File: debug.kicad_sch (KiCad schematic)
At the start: 61 parts, among them J701 USB4105-GF-A, J702 Conn_02x10_Odd_Even, U701 USBLC6-2SC6, U702 FT231XQ-R, U703 TCA9554PW

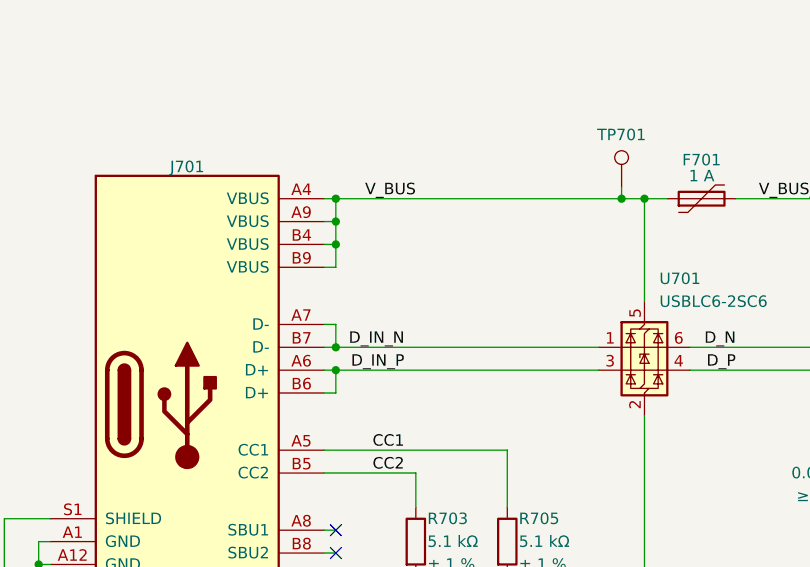
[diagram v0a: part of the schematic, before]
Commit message: Redo MPU pinout using STM32CubeMx
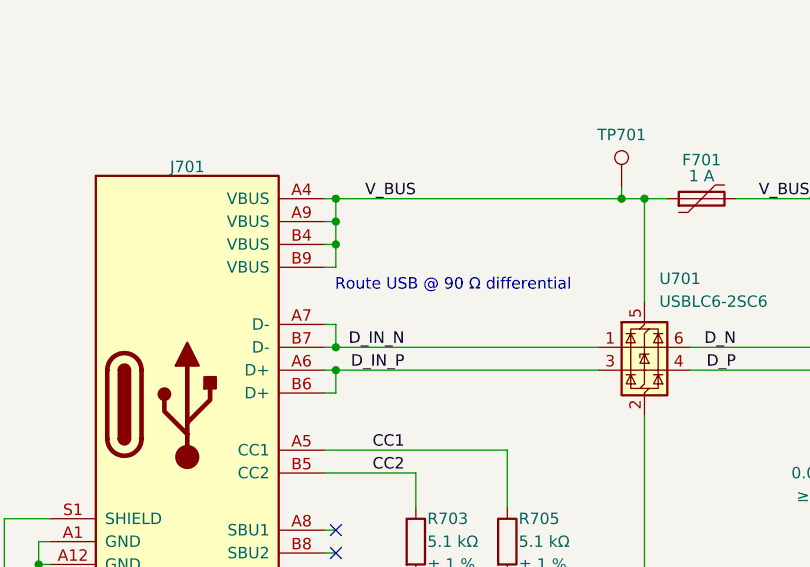
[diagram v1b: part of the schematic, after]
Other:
- note added: "Route USB @ 90 Ω differential"
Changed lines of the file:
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@@
 		(rev "v0.0.1")
+	)
+	(text "Route USB @ 90 Ω differential"
+		(exclude_from_sim no)
+		(at 80.772 200.152 0)
+		(effects
+			(font
+				(size 1.27 1.27)
+				(color 194 0 194 1)
+			)
+			(justify right)
+		)
 	)
 	(text_box "There are 4 debug LEDs; two RGB LEDs and two red LEDs."

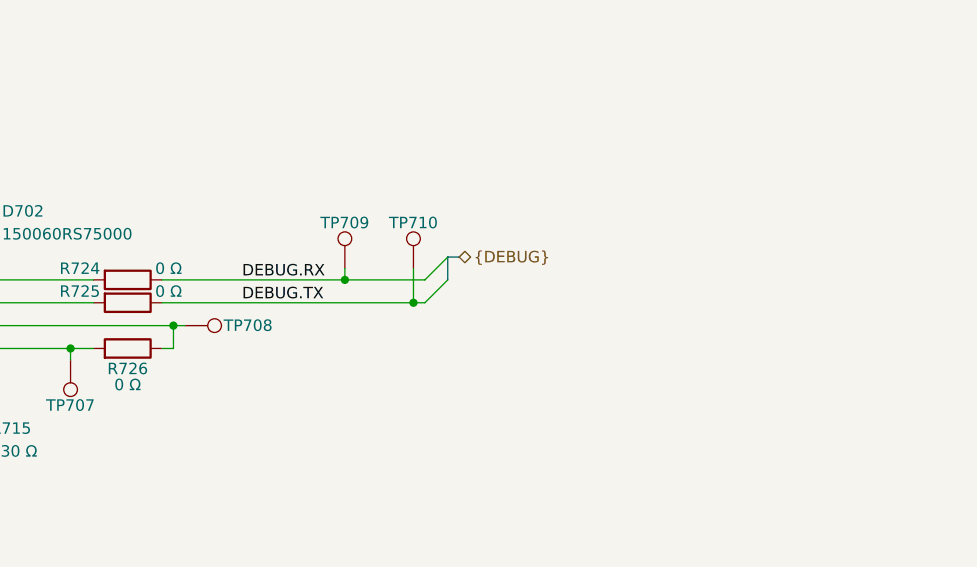
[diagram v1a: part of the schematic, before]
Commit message: Add debug VCOM port 0 ohm pokayoke
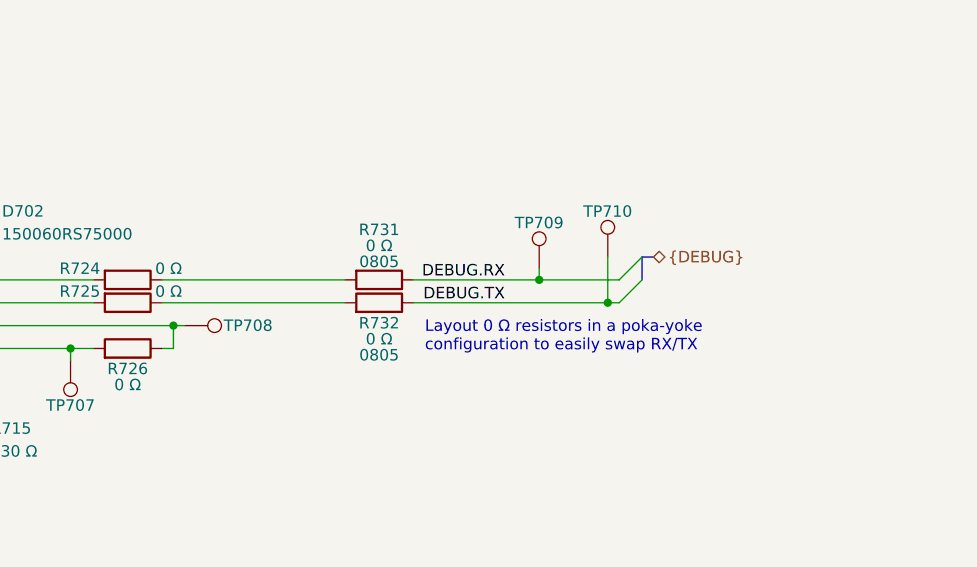
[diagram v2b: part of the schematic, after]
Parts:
- added R724: 0 Ω, perfect_footprints:R_0402_1005Metric, symbol Device:R
- added R732: 0 Ω, Resistor_SMD:R_0805_2012Metric, symbol Device:R
- R731: renamed from R724; footprint perfect_footprints:R_0402_1005Metric -> Resistor_SMD:R_0805_2012Metric; MPN 560112110020 -> (none); Manufacturer Würth Elektronik -> (none); Size (none) -> 0805
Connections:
- net DEBUG.TX: now also R732.1; no longer R725.1
- net TXD: now also R724.2; no longer R731.2
- new net: R725.1, R732.2
- new net: R724.1, R731.2
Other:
- note added: "Layout 0 Ω resistors in a poka-yoke configuration to easily swap RX/TX"
- moved on the sheet: R731, TP709, TP710

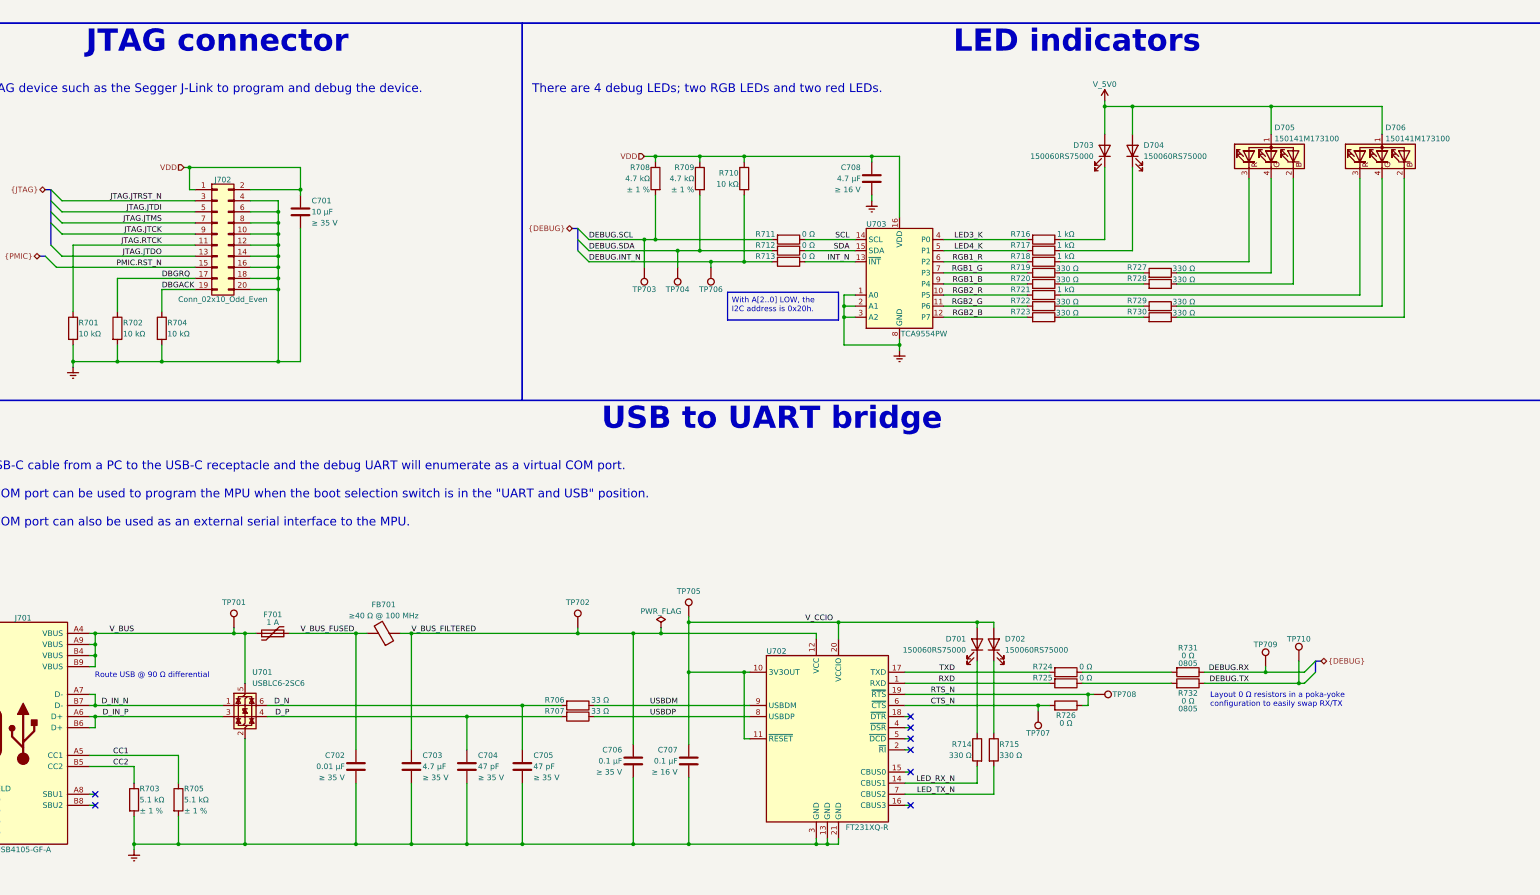
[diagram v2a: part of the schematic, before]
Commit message: Add additional info to passives
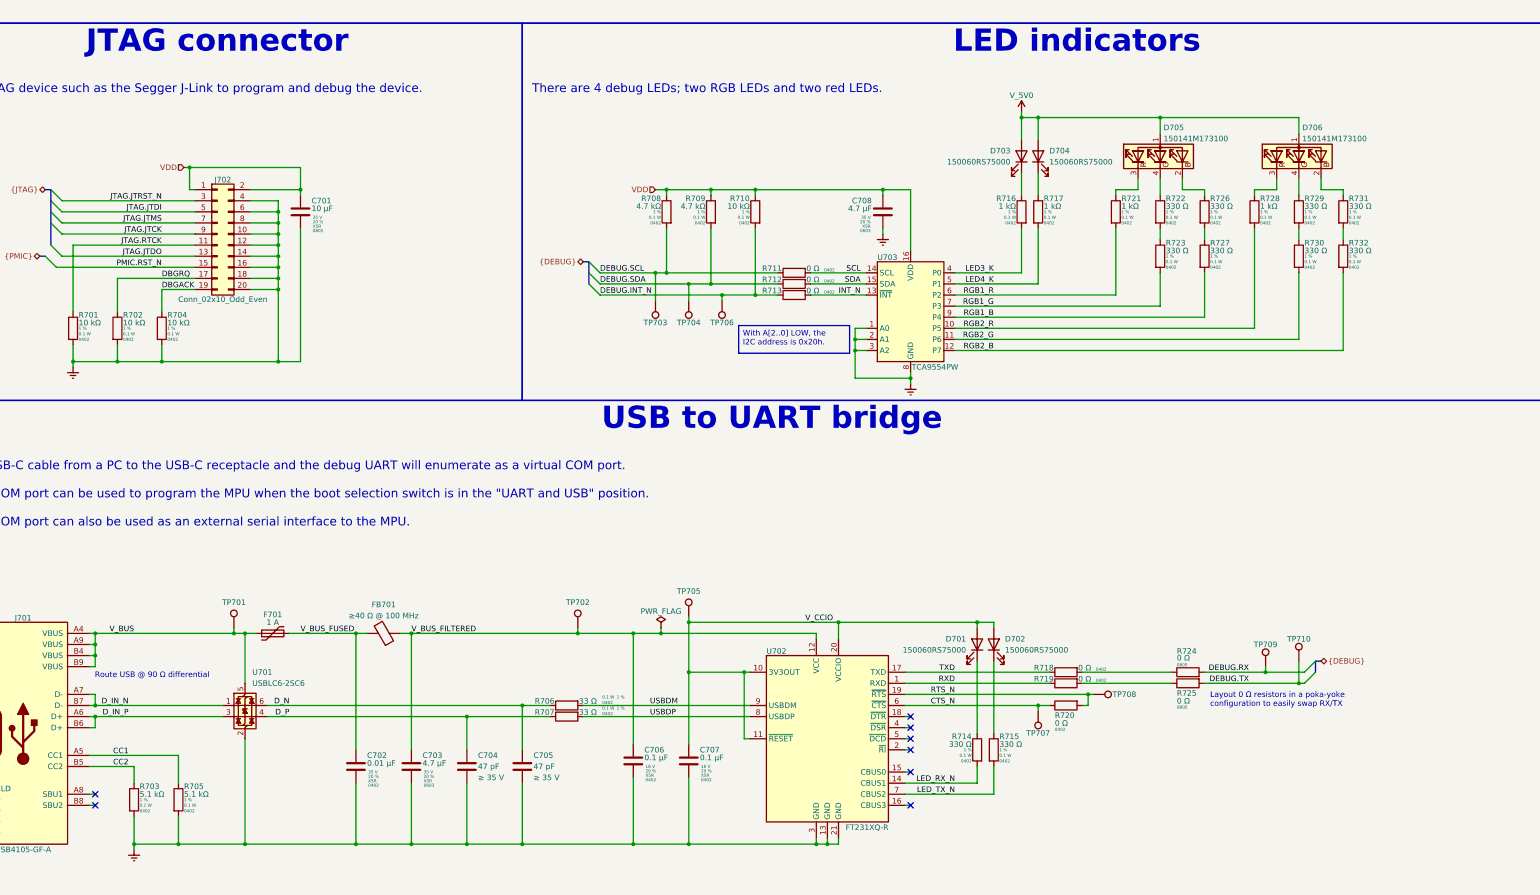
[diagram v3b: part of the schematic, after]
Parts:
- C701: footprint Capacitor_SMD:C_0603_1608Metric -> (none); MPN GRM188R6YA106MA73D -> (none); Manufacturer Murata Electronics -> (none); Size (none) -> 0805; Temperature coefficient (none) -> X5R; Tolerance (none) -> 20 %; Voltage rating ≥ 35 V -> 35 V
- C702: Size (none) -> 0402; Temperature coefficient (none) -> X5R; Tolerance (none) -> 20 %; Voltage rating ≥ 35 V -> 35 V
- C703: footprint Capacitor_SMD:C_0603_1608Metric -> (none); MPN GRM188R6YA475KE15D -> (none); Manufacturer Murata Electronics -> (none); Size (none) -> 0603; Temperature coefficient (none) -> X5R; Tolerance (none) -> 20 %; Voltage rating ≥ 35 V -> 35 V
- C706: Size (none) -> 0402; Temperature coefficient (none) -> X5R; Tolerance (none) -> 20 %; Voltage rating ≥ 35 V -> 16 V
- C707: Size (none) -> 0402; Temperature coefficient (none) -> X5R; Tolerance (none) -> 20 %; Voltage rating ≥ 16 V -> 16 V
- C708: footprint Capacitor_SMD:C_0603_1608Metric -> (none); MPN GRM188R6YA475KE15D -> (none); Manufacturer Murata Electronics -> (none); Size (none) -> 0603; Temperature coefficient (none) -> X5R; Tolerance (none) -> 20 %; Voltage rating ≥ 16 V -> 35 V
- R701, R702, R704, R706, R707, R710, R716, R717, R721: MPN 560112110020 -> (none); Manufacturer Würth Elektronik -> (none); Power rating (none) -> 0.1 W; Size (none) -> 0402; Tolerance (none) -> 1 %
- R703, R705, R708, R709: Power rating (none) -> 0.1 W; Size (none) -> 0402; Tolerance ± 1 % -> 1 %
- R711, R712, R713: footprint perfect_footprints:R_0402_1005Metric -> (none); MPN 560112110020 -> (none); Manufacturer Würth Elektronik -> (none); Size (none) -> 0402
- R714, R715, R722, R723, R727, R729, R730: MPN 560112110019 -> (none); Manufacturer Würth Elektronik -> (none); Power rating (none) -> 0.1 W; Size (none) -> 0402; Tolerance (none) -> 1 %
- R718: value 1 kΩ -> 0 Ω; footprint perfect_footprints:R_0402_1005Metric -> (none); MPN 560112110020 -> (none); Manufacturer Würth Elektronik -> (none); Size (none) -> 0402
- R719, R720: value 330 Ω -> 0 Ω; footprint perfect_footprints:R_0402_1005Metric -> (none); MPN 560112110019 -> (none); Manufacturer Würth Elektronik -> (none); Size (none) -> 0402
- R724, R725: footprint perfect_footprints:R_0402_1005Metric -> (none); MPN 560112110020 -> (none); Manufacturer Würth Elektronik -> (none); Size (none) -> 0805
- R726: value 0 Ω -> 330 Ω; footprint Resistor_SMD:R_0805_2012Metric -> perfect_footprints:R_0402_1005Metric; MPN 560112120002 -> (none); Manufacturer Würth Elektronik -> (none); Power rating (none) -> 0.1 W; Size (none) -> 0402; Tolerance (none) -> 1 %
- R728: value 330 Ω -> 1 kΩ; MPN 560112110019 -> (none); Manufacturer Würth Elektronik -> (none); Power rating (none) -> 0.1 W; Size (none) -> 0402; Tolerance (none) -> 1 %
- R731, R732: value 0 Ω -> 330 Ω; footprint Resistor_SMD:R_0805_2012Metric -> perfect_footprints:R_0402_1005Metric; Power rating (none) -> 0.1 W; Size 0805 -> 0402; Tolerance (none) -> 1 %
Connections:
- net CTS_N: now also R720.1; no longer R726.2
- net DEBUG.INT_N: now also R713.1; no longer R713.2
- net DEBUG.RX: now also R724.2; no longer R731.1
- net DEBUG.SCL: now also R711.1; no longer R711.2
- net DEBUG.SDA: now also R712.1; no longer R712.2
- net DEBUG.TX: now also R725.2; no longer R732.1
- net D_N: now also R706.1; no longer R706.2
- net D_P: now also R707.1; no longer R707.2
- net INT_N: now also R713.2; no longer R713.1
- net RGB1_B: now also R727.2; no longer R720.2
- net RGB1_G: now also R723.2; no longer R719.2
- net RGB1_R: now also R721.2; no longer R718.2
- net RGB2_B: now also R732.2; no longer R723.2
- net RGB2_G: now also R730.2; no longer R722.2
- net RGB2_R: now also R728.2; no longer R721.2
- net RTS_N: now also R720.2; no longer R726.1
- net RXD: now also R719.1; no longer R725.2
- net SCL: now also R711.2; no longer R711.1
- net SDA: now also R712.2; no longer R712.1
- net TXD: now also R718.1; no longer R724.2
- net USBDM: now also R706.2; no longer R706.1
- net USBDP: now also R707.2; no longer R707.1
- net at R725.1: now also R719.2; no longer R732.2
- net at R722.1: now also D705.4 (GK); no longer R729.2
- net at D705.2 (BK): now also R726.1; no longer R728.1
- net at D705.3 (RK): now also R721.1; no longer R718.1
- net at R727.1: now also R726.2; no longer D705.4 (GK)
- net at R730.1: now also R729.2; no longer D706.2 (BK)
- net at R723.1: now also R722.2; no longer R730.2
- net at R724.1: now also R718.2; no longer R731.2
- net at D706.3 (RK): now also R728.1; no longer R721.1
- new net: R731.2, R732.1
- new net: D706.2 (BK), R731.1
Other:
- moved on the sheet: D703, D705, TP703, TP704, TP706, U703

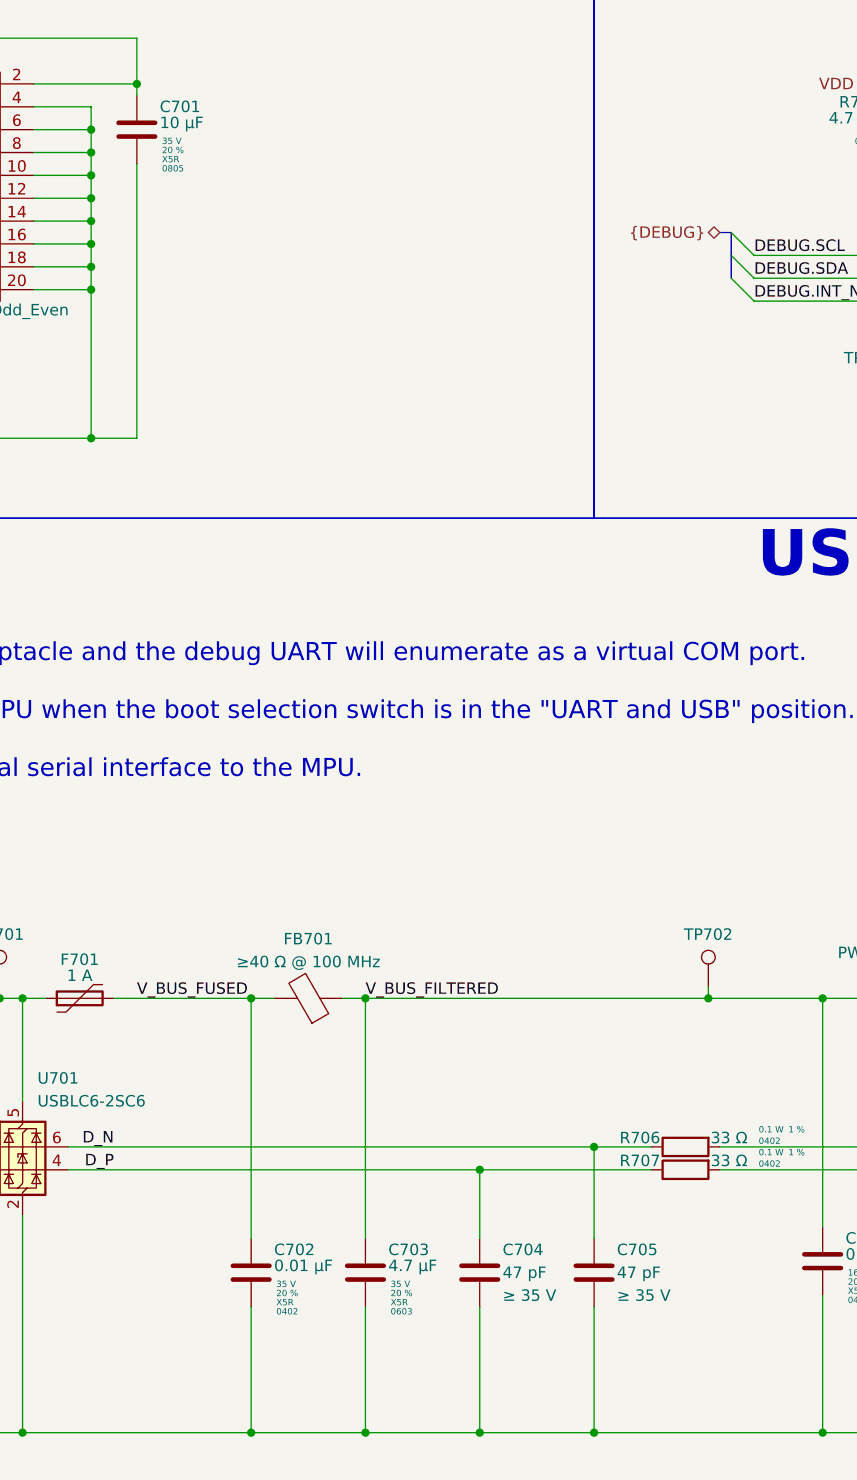
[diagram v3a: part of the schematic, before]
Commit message: Update capacitor BOM
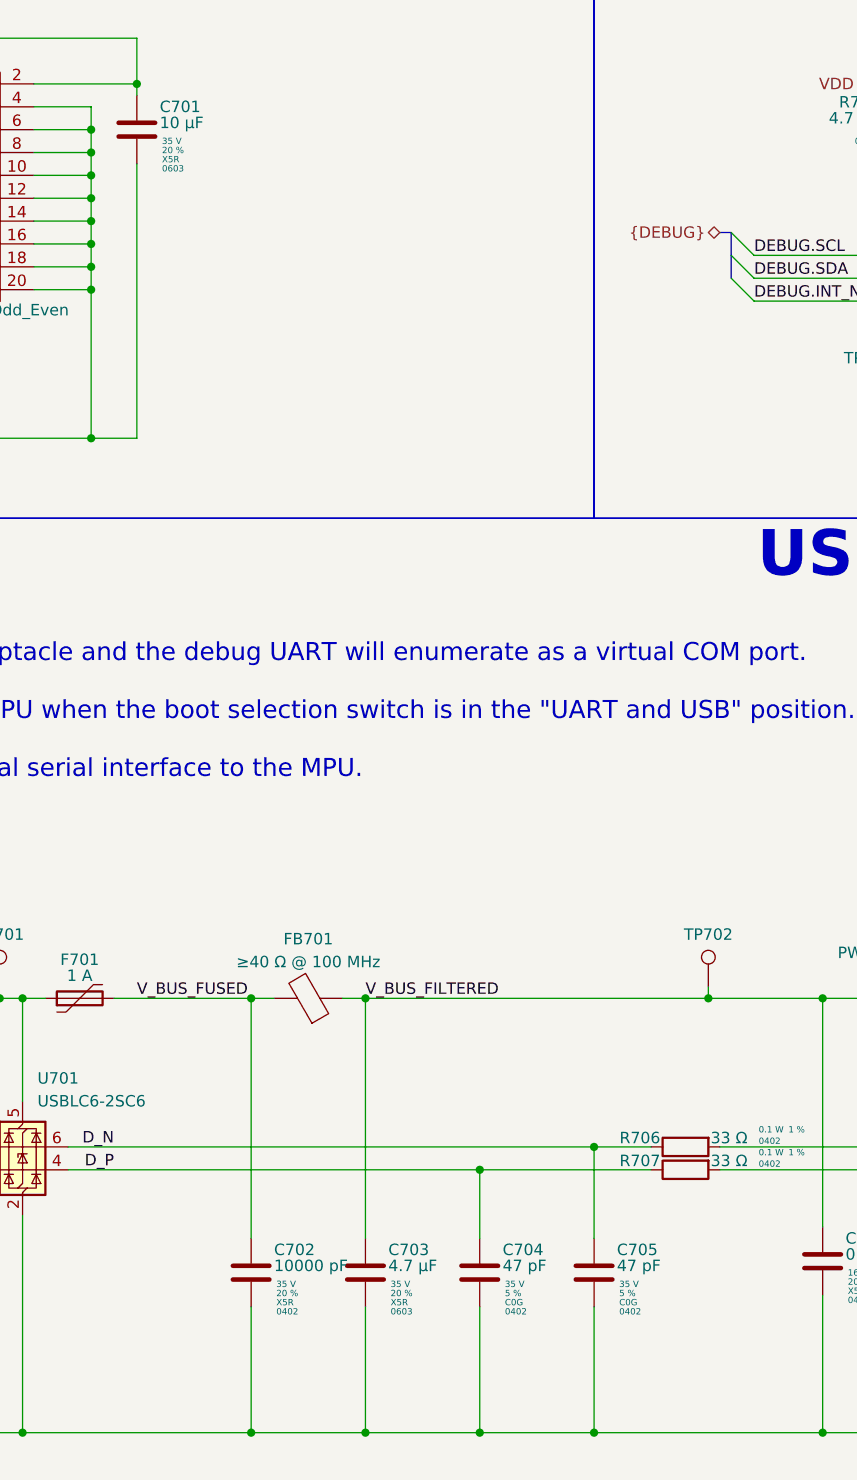
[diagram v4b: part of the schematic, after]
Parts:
- C701: footprint (none) -> Capacitor_SMD:C_0603_1608Metric; Digi-Key Part Number (none) -> 490-13248-1-ND; MPN (none) -> GRM188R6YA106MA73D; Manufacturer (none) -> Murata Electronics; Size 0805 -> 0603
- C702: value 0.01 µF -> 10000 pF; footprint (none) -> perfect_footprints:C_0402_1005Metric; Digi-Key Part Number (none) -> 490-4516-1-ND; MPN (none) -> GRM155R71H103KA88D; Manufacturer (none) -> Murata Electronics
- C703, C708: footprint (none) -> Capacitor_SMD:C_0603_1608Metric; Digi-Key Part Number (none) -> 490-7205-1-ND; MPN (none) -> GRM188R6YA475KE15D; Manufacturer (none) -> Murata Electronics
- C704, C705: footprint (none) -> perfect_footprints:C_0402_1005Metric; Digi-Key Part Number (none) -> 490-5942-1-ND; MPN (none) -> GRM1555C1H470JA01D; Manufacturer (none) -> Murata Electronics; Size (none) -> 0402; Temperature coefficient (none) -> C0G; Tolerance (none) -> 5 %; Voltage rating ≥ 35 V -> 35 V
- C706, C707: footprint (none) -> perfect_footprints:C_0402_1005Metric; Digi-Key Part Number (none) -> 490-10700-1-ND; MPN (none) -> GRM155R71H104KE14D; Manufacturer (none) -> Murata Electronics
